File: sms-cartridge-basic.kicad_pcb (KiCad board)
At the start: 2 copper layers, 65 x 38.5 mm, 0 parts

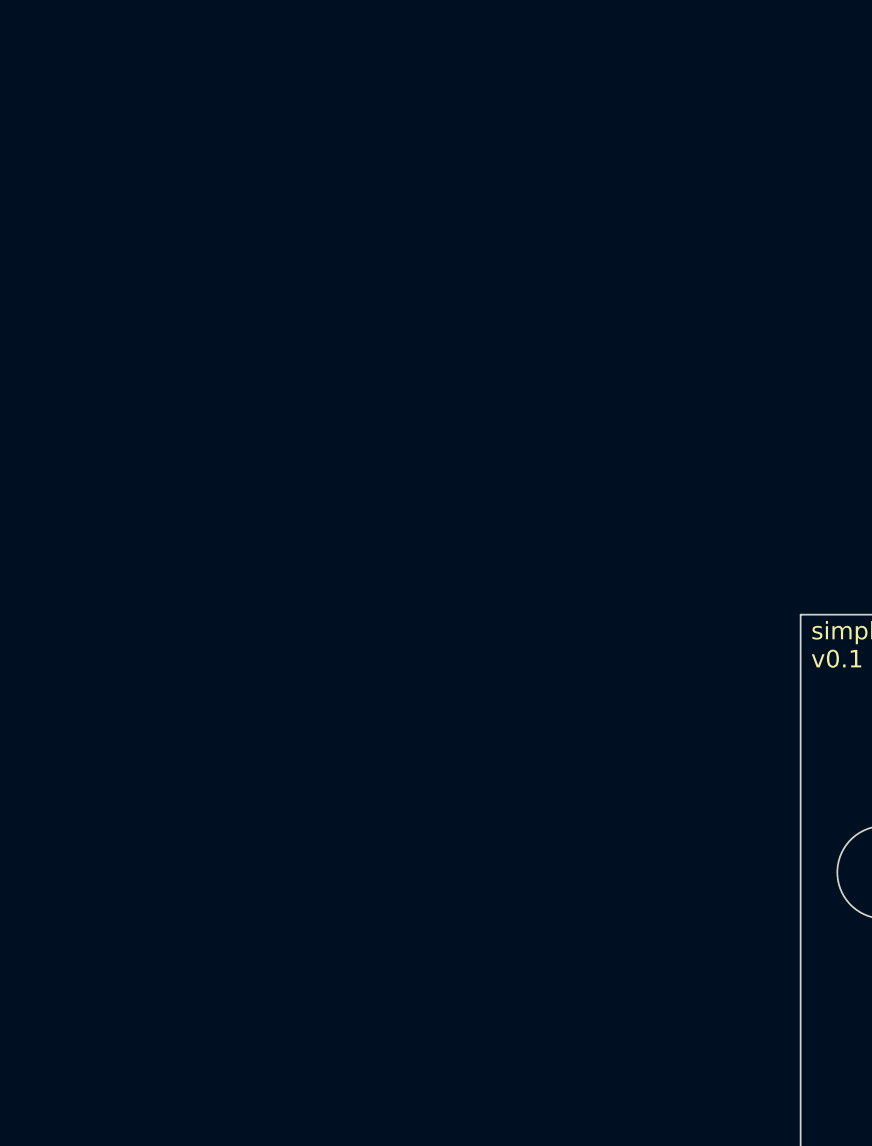
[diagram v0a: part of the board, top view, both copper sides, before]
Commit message: Edge connector symbol, basic schematic
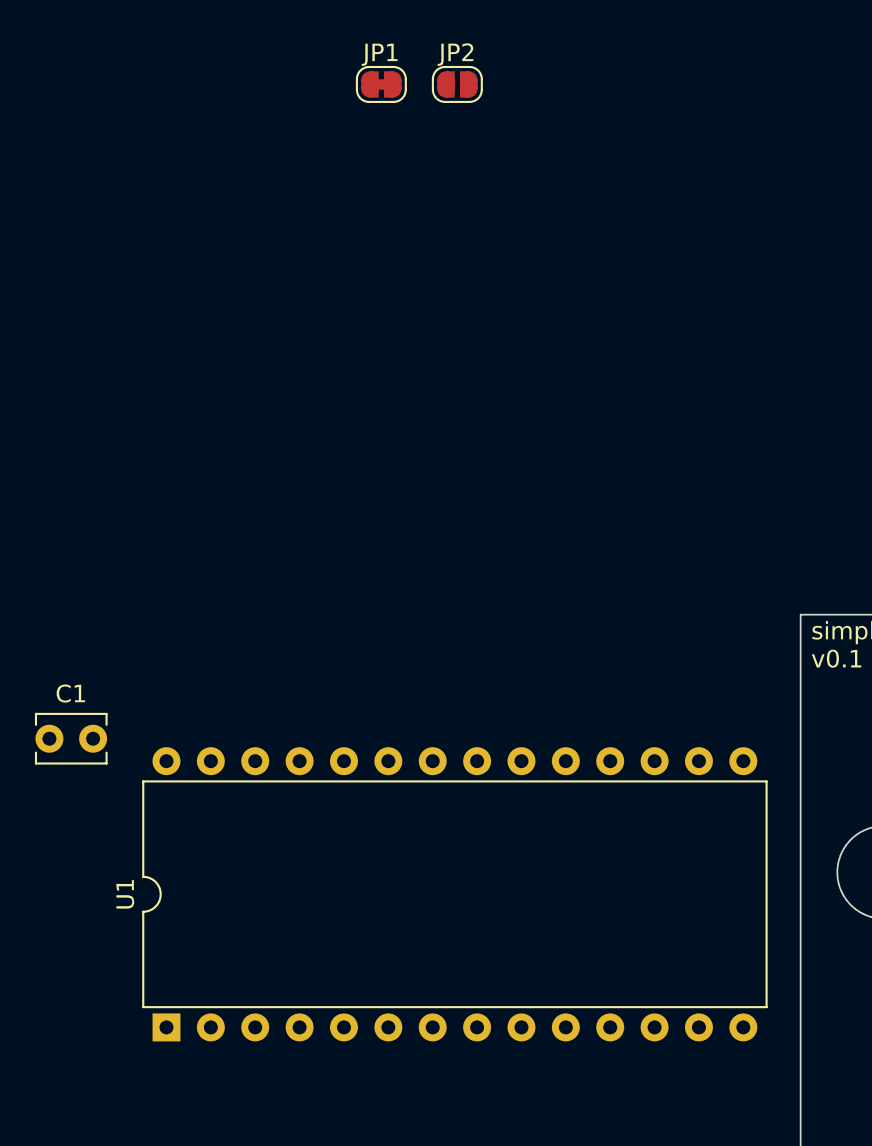
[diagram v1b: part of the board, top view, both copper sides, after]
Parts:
- added C1: 0.1µF, Capacitor_THT:C_Disc_D3.8mm_W2.6mm_P2.50mm, F.Cu at (57.0, 62.1)
- added JP1: Jumper_2_Bridged, Jumper:SolderJumper-2_P1.3mm_Bridged_RoundedPad1.0x1.5mm, F.Cu at (76.0, 24.6)
- added JP2: Jumper_2_Open, Jumper:SolderJumper-2_P1.3mm_Open_RoundedPad1.0x1.5mm, F.Cu at (80.3, 24.6)
- added U1: 27C256, Package_DIP:DIP-28_W15.24mm, F.Cu at (63.7, 78.6)

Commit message: v0.1
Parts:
- added REF**: OSHW-Logo2_9.8x8mm_SilkScreen, Symbol:OSHW-Logo2_9.8x8mm_SilkScreen, F.Cu at (157.5, 71.6)
- added U2: SMSUCartEdge, MasterSystem:SMS_Cartridge, F.Cu at (163.0, 88.0)
- moved C1 92.1 mm to (148.6, 71.9), turned to -90 degrees
- moved U1 47.6 mm to (111.3, 76.5)
- moved JP1 46.1 mm to (105.2, 60.3)
- moved JP2 45.6 mm to (105.2, 62.9)
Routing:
- net /a14: track 0.00 -> 86.5 mm, vias 0 -> 2
- net /a13: track 0.00 -> 73.7 mm, vias 0 -> 2
- net /a8: track 0.00 -> 68.7 mm, vias 0 -> 3
- net /a9: track 0.00 -> 64.1 mm, vias 0 -> 2
- net /~{RD}: track 0.00 -> 63.8 mm, vias 0 -> 3
- net /a11: track 0.00 -> 59.0 mm, vias 0 -> 3
- net /a10: track 0.00 -> 54.1 mm, vias 0 -> 3
- net /~{CE}: track 0.00 -> 52.0 mm, vias 0 -> 2
- net /d7: track 0.00 -> 49.2 mm, vias 0 -> 3
- net /d6: track 0.00 -> 47.3 mm, vias 0 -> 2
- net /d5: track 0.00 -> 44.1 mm, vias 0 -> 3
- net /d4: track 0.00 -> 41.3 mm, vias 0 -> 2
- net /d3: track 0.00 -> 36.8 mm, vias 0 -> 3
- net GND: track 0.00 -> 23.2 mm, vias 0 -> 2
- net /a12: track 0.00 -> 16.7 mm
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- added copper zone on F.Cu, net +5V
- added copper zone on B.Cu, net GND
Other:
- board text added: "A14?"
- board text added: "a14"
- board text added: "gnd"
- board text added: "sockets may not fit in case"
- board text added: "~{CE}"
- board text added: "~{RD}"

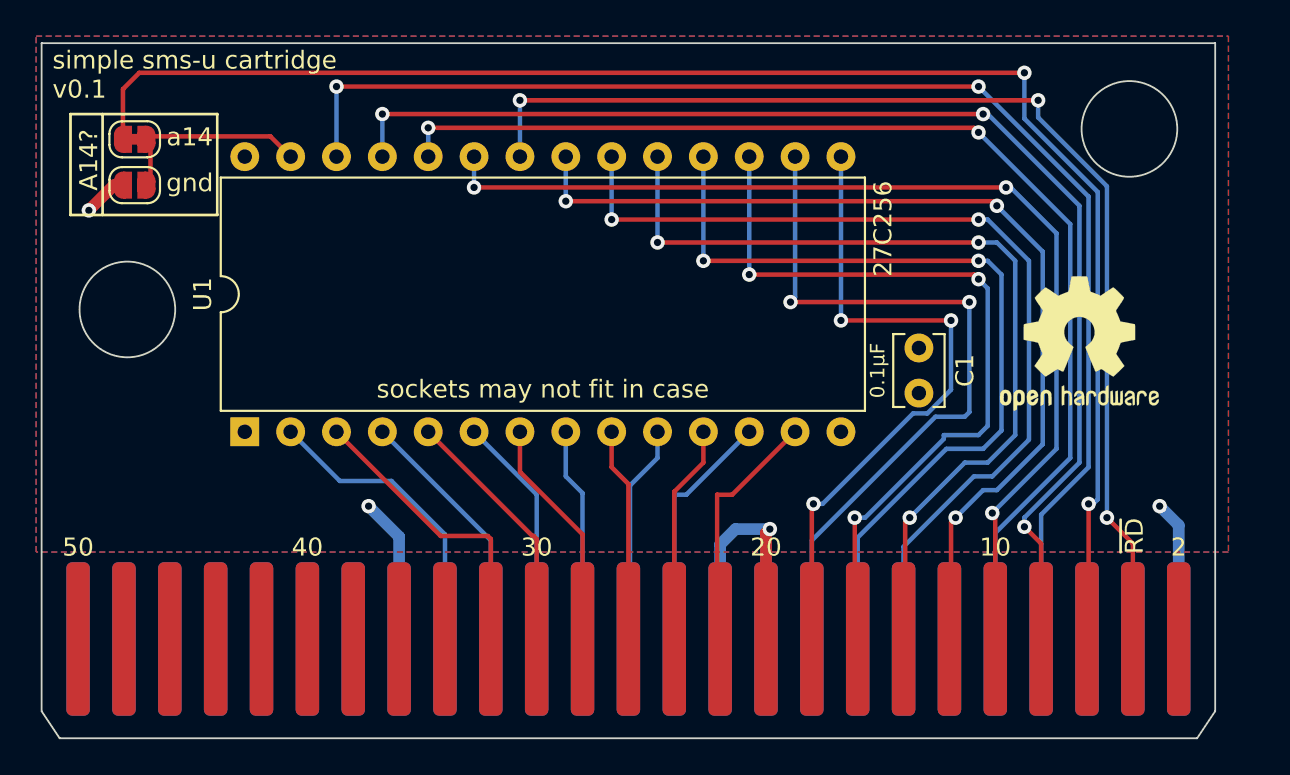
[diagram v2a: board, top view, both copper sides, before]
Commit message: Wider (0.8mm measurement error), wider teeth
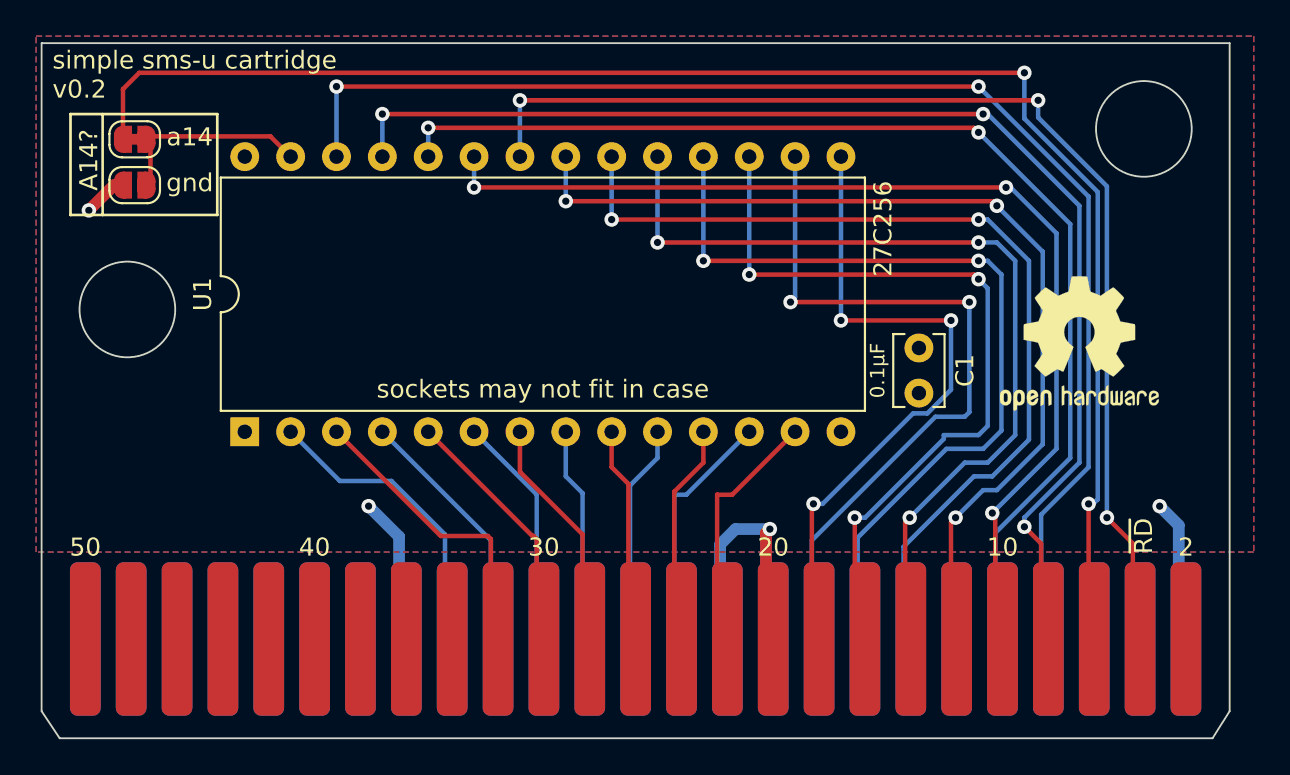
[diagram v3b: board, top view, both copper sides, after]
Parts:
- moved U2 0.40 mm to (163.4, 88.0)
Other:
- board size 65 x 38.5 mm -> 65.8 x 38.5 mm
- board text added: "simple sms-u cartridge v0.2"
- board text removed: "simple sms-u cartridge v0.1"

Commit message: Bodge to M0-7
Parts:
- removed REF**: OSHW-Logo2_9.8x8mm_SilkScreen, Symbol:OSHW-Logo2_9.8x8mm_SilkScreen
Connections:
- U1 pad 22: /~{RD} -> /~{M0-7}
- U2 pad 11: unconnected-(U2-Pad11) -> /~{M0-7}
- U2 pad 4: /~{RD} -> unconnected-(U2-Pad4)
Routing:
- net /~{RD}: track 63.8 -> 0.00 mm, vias 3 -> 0
- net /~{M0-7}: track 0.00 -> 56.6 mm, vias 0 -> 2
- net /~{CE}: track 52.0 -> 51.4 mm
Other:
- board text added: "simple sms-u cartridge v0.3"
- board text added: "~{M0-7}"
- board text added: "~{OE}"
- board text removed: "simple sms-u cartridge v0.2"
